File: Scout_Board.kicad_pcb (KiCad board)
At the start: 2 copper layers, 102.5 x 80 mm, 57 parts, among them J1 Conn_01x01_Pin, J2 Conn_01x04_Pin, J3 RAPC722X, J4 Screw_Terminal_01x02, J5 5V, J6 GND, Q1 BSS138, Q2 BSS138, U1 DRV8871DDA, U2 ESP32-S3-DEVKITC-1U-N8R2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

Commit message: New Branch - Alpha2.0
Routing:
- net RxD: track 41.0 -> 40.0 mm

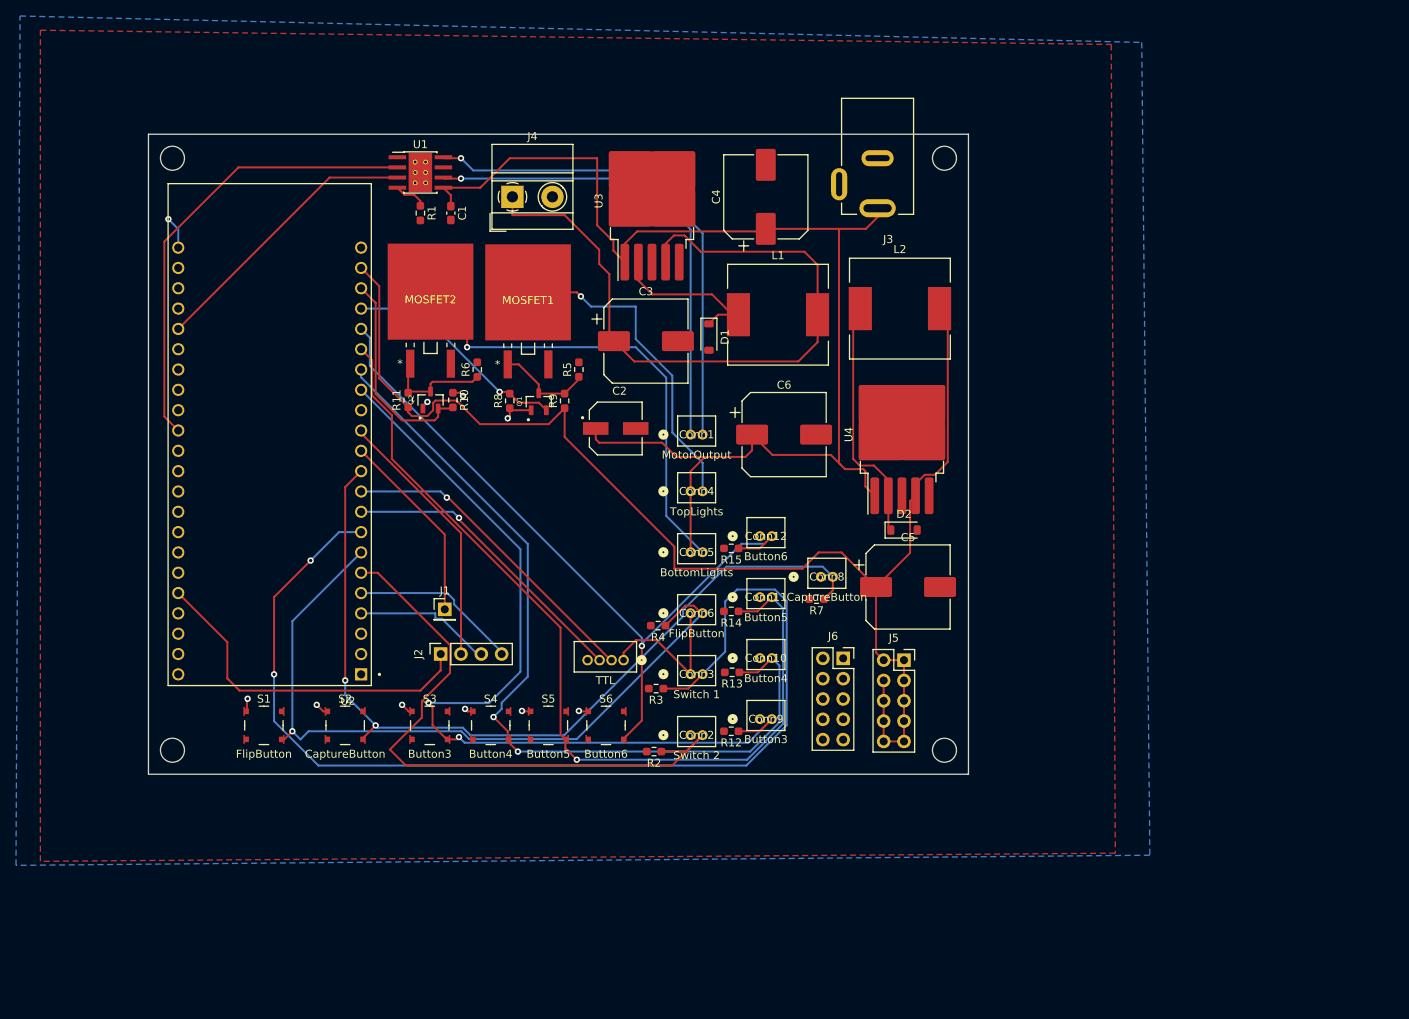
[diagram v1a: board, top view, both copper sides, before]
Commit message: power board changes
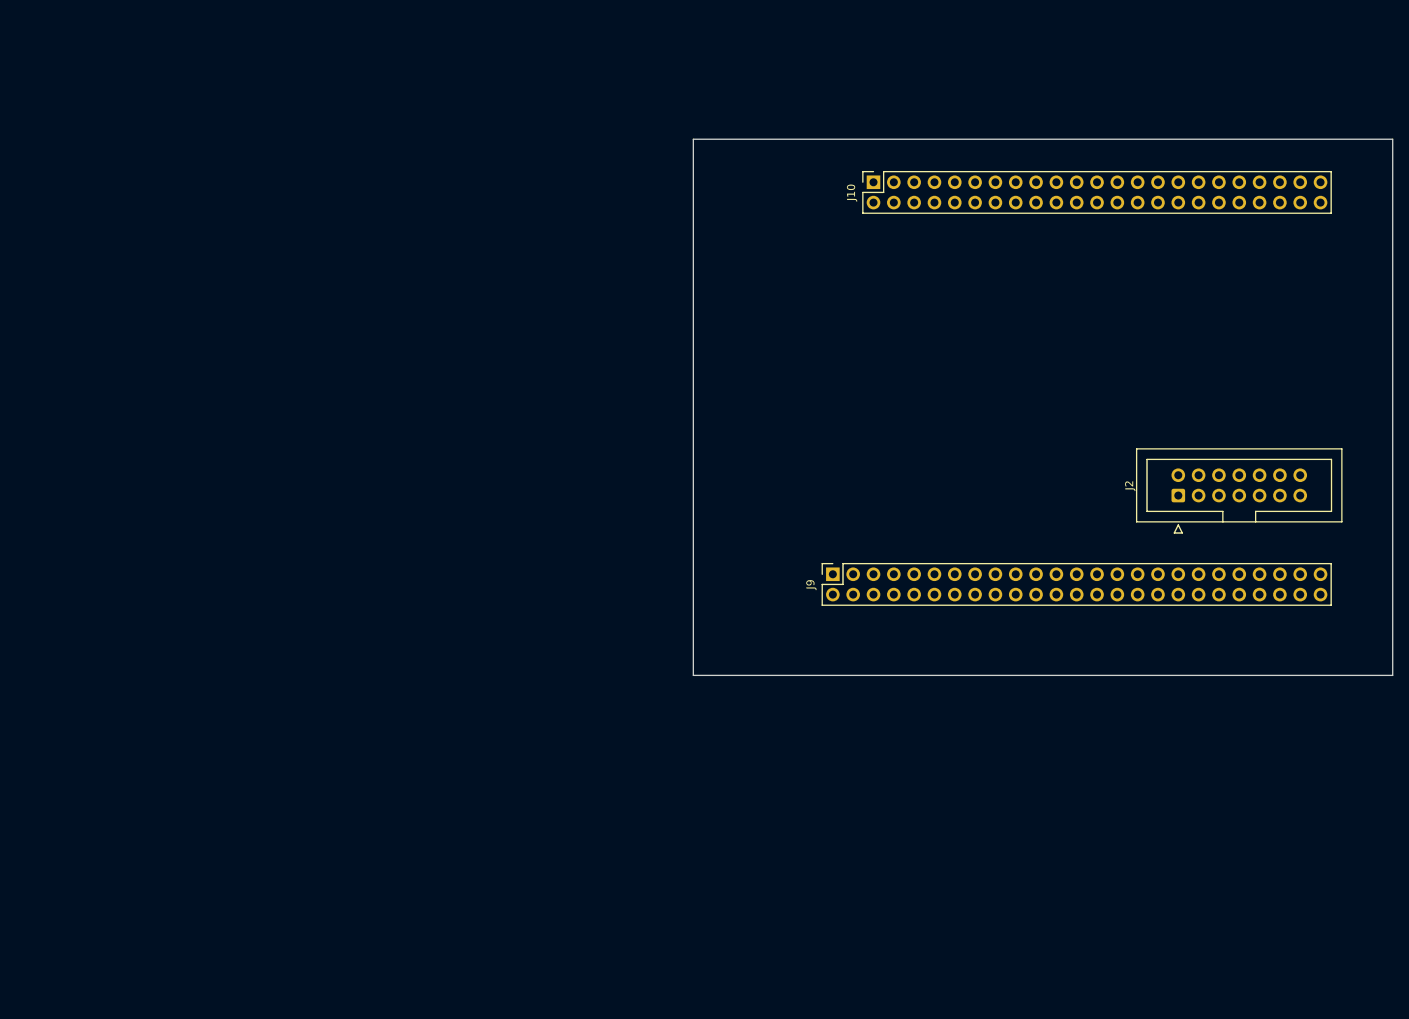
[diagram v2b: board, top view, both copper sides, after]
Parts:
- removed C1: 0.1uF/50V, Capacitor_SMD:C_0603_1608Metric_Pad1.08x0.95mm_HandSolder
- removed C2: 22uF/63V, EEH_ZA1J220XP:CAP_EEHZA1J220XP
- removed C3, C5: 220uF/35V, Capacitor_SMD:CP_Elec_10x10
- removed C4, C6: 100uF/63V, Capacitor_SMD:CP_Elec_10x10
- removed Conn1: MotorOutput, Downloaded_footprints:CONN_B2B-ZRLFSN_JST
- removed Conn10: Button4, Downloaded_footprints:CONN_B2B-ZRLFSN_JST
- removed Conn11: Button5, Downloaded_footprints:CONN_B2B-ZRLFSN_JST
- removed Conn12: Button6, Downloaded_footprints:CONN_B2B-ZRLFSN_JST
- removed Conn2: Switch 2, Downloaded_footprints:CONN_B2B-ZRLFSN_JST
- removed Conn3: Switch 1, Downloaded_footprints:CONN_B2B-ZRLFSN_JST
- removed Conn4: TopLights, Downloaded_footprints:CONN_B2B-ZRLFSN_JST
- removed Conn5: BottomLights, Downloaded_footprints:CONN_B2B-ZRLFSN_JST
- removed Conn6: FlipButton, Downloaded_footprints:CONN_B2B-ZRLFSN_JST
- removed Conn7: TTL, Downloaded_footprints:CONN_B4B-ZRLFSN_JST
- removed Conn8: CaptureButton, Downloaded_footprints:CONN_B2B-ZRLFSN_JST
- removed Conn9: Button3, Downloaded_footprints:CONN_B2B-ZRLFSN_JST
- removed D1, D2: 1N5819HW-7-F, Diode_SMD:D_SOD-123
- removed J1: Conn_01x01_Pin, Connector_PinHeader_2.54mm:PinHeader_1x01_P2.54mm_Vertical
- removed J3: RAPC722X, Downloaded_footprints:SWITCHCRAFT_RAPC722X
- removed J4: Screw_Terminal_01x02, TerminalBlock_MetzConnect:TerminalBlock_MetzConnect_Type011_RT05502HBWC_1x02_P5.00mm_Horizontal
- removed J5: 5V, Connector_PinSocket_2.54mm:PinSocket_2x05_P2.54mm_Vertical
- removed J6: GND, Connector_PinSocket_2.54mm:PinSocket_2x05_P2.54mm_Vertical
- removed L1, L2: 47uH, Inductor_SMD:L_12x12mm_H8mm
- removed MOSFET1, MOSFET2: IRFZ44NSTRLPBF, Downloaded_footprints:D2PAK_INF
- removed Q1, Q2: BSS138, Downloaded_footprints:SOT95P240X111-3N
- removed R1: 30k, Resistor_SMD:R_0603_1608Metric_Pad0.98x0.95mm_HandSolder
- removed R10, R11, R12, R13, R14, R15, R2, R3, R4, R7, R8, R9: 10k, Resistor_SMD:R_0603_1608Metric_Pad0.98x0.95mm_HandSolder
- removed R5, R6: 1M, Resistor_SMD:R_0603_1608Metric_Pad0.98x0.95mm_HandSolder
- removed S1: FlipButton, digikey-footprints:Switch_Tactile_SMD_4.5x4.5mm_TL3315NF160Q
- removed S2: CaptureButton, digikey-footprints:Switch_Tactile_SMD_4.5x4.5mm_TL3315NF160Q
- removed S3: Button3, digikey-footprints:Switch_Tactile_SMD_4.5x4.5mm_TL3315NF160Q
- removed S4: Button4, digikey-footprints:Switch_Tactile_SMD_4.5x4.5mm_TL3315NF160Q
- removed S5: Button5, digikey-footprints:Switch_Tactile_SMD_4.5x4.5mm_TL3315NF160Q
- removed S6: Button6, digikey-footprints:Switch_Tactile_SMD_4.5x4.5mm_TL3315NF160Q
- removed U1: DRV8871DDA, Package_SO:Texas_HTSOP-8-1EP_3.9x4.9mm_P1.27mm_EP2.95x4.9mm_Mask2.4x3.1mm_ThermalVias
- removed U2: ESP32-S3-DEVKITC-1U-N8R2, Downloaded_footprints:XCVR_ESP32-S3-DEVKITC-1U-N8R2
- removed U3, U4: LM2576HVS-5, Package_TO_SOT_SMD:TO-263-5_TabPin3
- added J10: BBAI_P8, Connector_PinSocket_2.54mm:PinSocket_2x23_P2.54mm_Vertical, F.Cu at (226.1, 95.5)
- added J9: BBAI_P9, Connector_PinSocket_2.54mm:PinSocket_2x25_P2.54mm_Vertical, F.Cu at (221.0, 144.5)
- J2: value Conn_01x04_Pin -> Conn_02x07_Odd_Even; footprint Connector_PinSocket_2.54mm:PinSocket_1x04_P2.54mm_Vertical -> Connector_IDC:IDC-Header_2x07_P2.54mm_Vertical
- moved J2 94.3 mm to (264.2, 134.6)
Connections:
- J2 pad 1: Conn1 -> Sw1
- J2 pad 2: Conn2 -> Sw2
- J2 pad 3: Conn3 -> Sw1b
- J2 pad 4: Conn4 -> Sw1b
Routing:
- net +5V: track 169.3 -> 0.00 mm
- net +12V: track 160.4 -> 0.00 mm
- net Sw1: track 138.5 -> 0.00 mm, vias 2 -> 0
- net Button5: track 111.4 -> 0.00 mm, vias 1 -> 0
- net Button3: track 109.2 -> 0.00 mm, vias 2 -> 0
- net CaptureButton: track 107.3 -> 0.00 mm, vias 2 -> 0
- net Button4: track 106.8 -> 0.00 mm, vias 2 -> 0
- net Button6: track 93.7 -> 0.00 mm, vias 1 -> 0
- net FlipButton: track 92.9 -> 0.00 mm, vias 1 -> 0
- net +5VA: track 87.5 -> 0.00 mm
- net Sw2: track 78.5 -> 0.00 mm
- net OUT2: track 61.5 -> 0.00 mm, vias 1 -> 0
- net OUT1: track 59.2 -> 0.00 mm, vias 1 -> 0
- net Net-(Conn5-Pin_2): track 59.0 -> 0.00 mm, vias 1 -> 0
- net IN2: track 57.3 -> 0.00 mm
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- removed copper zone on B.Cu, net +3.3V
- removed copper zone on F.Cu, net GND
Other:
- board size 102.5 x 80 mm -> 87.4 x 67 mm

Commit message: New board test
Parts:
- added C1: 100uF/16V, Capacitor_SMD:CP_Elec_6.3x5.9, F.Cu at (147.0, 169.5)
- added Conn2: CaptureButton, Connector_JST:JST_XH_B2B-XH-AM_1x02_P2.50mm_Vertical, F.Cu at (240.5, 173.0)
- added Conn4: FlipButton, Connector_JST:JST_XH_B2B-XH-AM_1x02_P2.50mm_Vertical, F.Cu at (240.5, 183.0)
- added J1: Conn_01x04_Pin, Connector_PinSocket_2.54mm:PinSocket_1x04_P2.54mm_Vertical, F.Cu at (217.0, 167.4)
- added J11: BBAI_P8, Connector_PinSocket_2.54mm:PinSocket_2x23_P2.54mm_Vertical, F.Cu at (177.8, 182.9)
- added J5: 5V, Connector_PinSocket_2.54mm:PinSocket_2x05_P2.54mm_Vertical, F.Cu at (224.8, 165.9)
- added J6: GND, Connector_PinSocket_2.54mm:PinSocket_2x05_P2.54mm_Vertical, F.Cu at (232.0, 165.9)
- added J7: IN, RAPC722X:SWITCHCRAFT_RAPC722X, F.Cu at (238.2, 145.8)
- added MOSFET1: IRFZ44NSTRLPBF, IRFZ44NSTRLPBF:DPAK254P1524X483-3N, B.Cu at (184.6, 151.0)
- added MOSFET2: IRFZ44NSTRLPBF, IRFZ44NSTRLPBF:DPAK254P1524X483-3N, B.Cu at (197.0, 151.0)
- added Q1: BSS138, BSS138:SOT95P240X111-3N, B.Cu at (164.9, 152.6)
- added Q2: BSS138, BSS138:SOT95P240X111-3N, B.Cu at (164.9, 157.0)
- added R1: 10k, Resistor_SMD:R_0603_1608Metric_Pad0.98x0.95mm_HandSolder, B.Cu at (235.0, 179.0)
- added R10: 1M, Resistor_SMD:R_0603_1608Metric_Pad0.98x0.95mm_HandSolder, B.Cu at (183.9, 161.3)
- added R11: 10k, Resistor_SMD:R_0603_1608Metric_Pad0.98x0.95mm_HandSolder, B.Cu at (169.1, 151.0)
- added R12: 10k, Resistor_SMD:R_0603_1608Metric_Pad0.98x0.95mm_HandSolder, B.Cu at (170.0, 159.0)
- added R13: 1M, Resistor_SMD:R_0603_1608Metric_Pad0.98x0.95mm_HandSolder, B.Cu at (197.0, 162.0)
- added R14: 10k, Resistor_SMD:R_0603_1608Metric_Pad0.98x0.95mm_HandSolder, B.Cu at (170.0, 156.0)
- added R2: 10k, Resistor_SMD:R_0603_1608Metric_Pad0.98x0.95mm_HandSolder, B.Cu at (236.0, 171.0)
- added R7: 10k, Resistor_SMD:R_0603_1608Metric_Pad0.98x0.95mm_HandSolder, B.Cu at (172.0, 175.1)
- added R8: 10k, Resistor_SMD:R_0603_1608Metric_Pad0.98x0.95mm_HandSolder, B.Cu at (172.0, 170.0)
- added R9: 10k, Resistor_SMD:R_0603_1608Metric_Pad0.98x0.95mm_HandSolder, B.Cu at (169.9, 153.0)
- added U1: ESP32-S3-DEVKITC-1U-N8R2, ESP32-S3-DEVKITC-1-N8R2:XCVR_ESP32-S3-DEVKITC-1-N8R2, F.Cu at (187.9, 152.5)
- added U2: ~, Module:Pololu_Breakout-16_15.2x20.3mm, F.Cu at (145.8, 188.0)
- J10: value BBAI_P8 -> BBAI_P9; footprint Connector_PinSocket_2.54mm:PinSocket_2x23_P2.54mm_Vertical -> Connector_PinSocket_2.54mm:PinSocket_2x25_P2.54mm_Vertical
- J9: value BBAI_P9 -> IN; footprint Connector_PinSocket_2.54mm:PinSocket_2x25_P2.54mm_Vertical -> RAPC722X:SWITCHCRAFT_RAPC722X
- moved J2 93.1 mm to (180.3, 175.0)
- moved J10 42.4 mm to (233.7, 137.2), turned to -90 degrees
- moved J9 22.4 mm to (238.2, 158.8)
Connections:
- net BLb renamed +12V
- J2 pad 3: Sw1b -> 5V
- J2 pad 4: Sw1b -> 5V
- J9 pad 1: unconnected-(J9-GND-Pad1) -> 5V
- J9 pad 2: unconnected-(J9-GND-Pad2) -> GND
- J9 pad 3: unconnected-(J9-3.3V-Pad3) -> GND
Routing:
- net TLa: track 0.00 -> 48.0 mm
- net 2B: track 0.00 -> 45.3 mm
- net BottomLightsHV: track 0.00 -> 43.6 mm
- net 2A: track 0.00 -> 40.1 mm
- net BLa: track 0.00 -> 35.2 mm
- net 1A: track 0.00 -> 34.4 mm
- net TopLightsHV: track 0.00 -> 33.2 mm
- net GND: track 0.00 -> 30.7 mm
- net +3.3V: track 0.00 -> 29.5 mm, vias 0 -> 1
- net 1B: track 0.00 -> 29.0 mm
- net Sw2: track 0.00 -> 8.94 mm
- net FlipButton: track 0.00 -> 8.74 mm
- net Sw1: track 0.00 -> 8.64 mm
- net CaptureButton: track 0.00 -> 8.21 mm
- net +12V: track 0.00 -> 6.98 mm
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- added copper zone on F.Cu, net +12V
- added copper zone on B.Cu, net +3.3V
- added copper zone on In1.Cu, net +3.3V
- added copper zone on In2.Cu, net 5V
- added copper zone on B.Cu, net GND
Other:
- board size 87.4 x 67 mm -> 104.2 x 65 mm
- copper layers 2 -> 4

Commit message: Layout changes
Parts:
- removed J5: 5V, Connector_PinSocket_2.54mm:PinSocket_2x05_P2.54mm_Vertical
- removed J6: GND, Connector_PinSocket_2.54mm:PinSocket_2x05_P2.54mm_Vertical
- removed J7, J9: IN, RAPC722X:SWITCHCRAFT_RAPC722X
- added J3: 705530002, 705530002:CONN3_53-0002_MOL, F.Cu at (254.0, 132.1)
- added MOSFET3: IRFZ44NSTRLPBF, IRFZ44NSTRLPBF:DPAK254P1524X483-3N, B.Cu at (180.3, 165.1)
- added Q3: BSS138, BSS138:SOT95P240X111-3N, B.Cu at (222.2, 160.5)
- added R29: 10k, Resistor_SMD:R_0603_1608Metric_Pad0.98x0.95mm_HandSolder, B.Cu at (225.6, 160.5)
- added R30: 1M, Resistor_SMD:R_0603_1608Metric_Pad0.98x0.95mm_HandSolder, B.Cu at (218.2, 158.6)
- added R31: 10k, Resistor_SMD:R_0603_1608Metric_Pad0.98x0.95mm_HandSolder, B.Cu at (218.2, 161.8)
- moved U2 101.9 mm to (247.7, 184.1)
- moved C1 99.2 mm to (246.1, 165.1)
- moved R7 90.1 mm to (256.9, 144.8), turned to 0 degrees
- moved R8 87.9 mm to (256.9, 147.3), turned to 0 degrees
- moved J2 75.0 mm to (248.9, 144.8), turned to -90 degrees
- moved Conn2 68.7 mm to (177.8, 144.8)
- moved Q1 60.3 mm to (221.7, 172.9)
- moved R9 59.1 mm to (225.6, 172.9), turned to -90 degrees
- moved Conn4 58.9 mm to (195.6, 144.8)
- moved Q2 57.6 mm to (221.7, 166.4)
- moved J1 57.1 mm to (170.2, 134.6)
- moved R2 56.2 mm to (185.7, 145.9)
- moved R12 56.0 mm to (225.5, 166.5), turned to -90 degrees
- moved J10 55.9 mm to (177.8, 134.5), turned to 90 degrees
- moved R11 54.0 mm to (218.0, 173.9), turned to 0 degrees
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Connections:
- J2 pad 11: +12V -> BL-
- J2 pad 13: unconnected-(J2-Pin_13-Pad13) -> UV-
- J2 pad 5: TLa -> +12V
- J2 pad 9: BLa -> TL-
- MOSFET1 pad 2: TLa -> TL-
- MOSFET2 pad 2: BLa -> BL-
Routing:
- net TL-: track 0.00 -> 114.6 mm
- net BL-: track 0.00 -> 96.0 mm
- net UV-: track 0.00 -> 64.1 mm
- net TLa: track 48.0 -> 0.00 mm
- net UVLightsHV: track 0.00 -> 45.6 mm
- net BLa: track 35.2 -> 0.00 mm
- net GND: track 30.7 -> 59.2 mm, vias 0 -> 4
- net TopLightsHV: track 33.2 -> 16.5 mm
- net 2B: track 45.3 -> 31.0 mm
- net BottomLightsHV: track 43.6 -> 31.1 mm
- net 2A: track 40.1 -> 31.0 mm
- net 1A: track 34.4 -> 31.0 mm
- net FlipButton: track 8.74 -> 5.35 mm
- net 5V: track 3.09 -> 0.00 mm, vias 2 -> 0
- net CaptureButton: track 8.21 -> 5.44 mm
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- added copper zone on In1.Cu, net +12V
- added copper zone on In2.Cu, net +3.3V
- added copper zone on B.Cu, net 5V
- added copper zone on F.Cu, net GND
- removed copper zone on F.Cu, net +12V
- removed copper zone on B.Cu, net +3.3V
- removed copper zone on In1.Cu, net +3.3V
- removed copper zone on In2.Cu, net 5V
- removed copper zone on B.Cu, net GND
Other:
- board size 104.2 x 65 mm -> 104.1 x 61 mm

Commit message: Layout updated with mounting holes
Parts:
- added J7: I2C, digikey-footprints:PinHeader_1x2_P2.5mm_Drill1.1mm, F.Cu at (170.4, 130.6)
- added J8: SPI, digikey-footprints:PinHeader_1x4_P2.5mm_Drill1.1mm, F.Cu at (245.6, 137.8)
- moved R7 28.9 mm to (228.6, 150.7), turned to -90 degrees
- moved R8 24.7 mm to (232.4, 150.7), turned to -90 degrees
- moved R11 13.1 mm to (230.2, 169.3), turned to 90 degrees
- moved R9 11.8 mm to (229.3, 161.8), turned to 0 degrees
- moved R30 10.9 mm to (215.0, 169.1), turned to -90 degrees
- moved Q1 10.5 mm to (229.3, 165.6), turned to -90 degrees
- moved R10 9.95 mm to (227.7, 169.4), turned to -90 degrees
- moved R29 8.72 mm to (216.9, 161.8), turned to 0 degrees
- moved R31 7.32 mm to (218.2, 169.1), turned to 90 degrees
- moved Q3 7.04 mm to (216.9, 165.1), turned to -90 degrees
- moved R13 6.26 mm to (224.0, 169.3), turned to -90 degrees
- moved R14 5.46 mm to (221.2, 169.3), turned to 90 degrees
- moved R12 5.39 mm to (222.9, 161.8), turned to 0 degrees
- moved J1 4.06 mm to (170.2, 138.7)
- moved Q2 1.39 mm to (222.8, 165.6), turned to -90 degrees
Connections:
- J10 pad 10: unconnected-(J10-Reset-Pad10) -> Sys_reset
- J10 pad 16: unconnected-(J10-GPIO0_94-Pad16) -> I2C1_SDA
- J10 pad 17: unconnected-(J10-GPIO0_28-Pad17) -> I2C1_SCL
- J10 pad 24: unconnected-(J10-GPIO0_119-Pad24) -> TxD
- J10 pad 26: unconnected-(J10-GPIO0_118-Pad26) -> RxD
- J10 pad 28: unconnected-(J10-GPIO1_11-Pad28) -> SPI1_CS0
- J10 pad 29: unconnected-(J10-GPIO1_14-Pad29) -> SPI1_D0
- J10 pad 30: unconnected-(J10-GPIO1_13-Pad30) -> SPI1_D1
- J10 pad 31: unconnected-(J10-GPIO1_12-Pad31) -> SPI1_SCLK
- J10 pad 43: unconnected-(J10-GND-Pad43) -> GND
- J10 pad 44: unconnected-(J10-GND-Pad44) -> GND
- J10 pad 45: unconnected-(J10-GND-Pad45) -> GND
- J10 pad 46: unconnected-(J10-GND-Pad46) -> GND
- J11 pad 1: unconnected-(J11-GND-Pad1) -> GND
- J11 pad 2: unconnected-(J11-GND-Pad2) -> GND
- J11 pad 7: unconnected-(J11-GPIO0_15-Pad7) -> SBC_Power
- J11 pad 8: unconnected-(J11-GPIO0_14-Pad8) -> Wire1
- J11 pad 9: unconnected-(J11-GPIO0_17-Pad9) -> Wire2
- J2 pad 1: Sw1 -> TL-
- J2 pad 11: BL- -> UV-
- J2 pad 13: UV- -> Sw1
- J2 pad 14: unconnected-(J2-Pin_14-Pad14) -> Sw2
- J2 pad 2: Sw2 -> unconnected-(J2-Pin_2-Pad2)
- J2 pad 9: TL- -> BL-
- U1 pad J1_12: unconnected-(U1-GPIO8-PadJ1_12) -> RxD
- U1 pad J1_13: unconnected-(U1-GPIO3-PadJ1_13) -> TxD
- U1 pad J1_14: unconnected-(U1-GPIO46-PadJ1_14) -> Sys_reset
- U1 pad J1_15: unconnected-(U1-GPIO9-PadJ1_15) -> Conn1
- U1 pad J1_16: unconnected-(U1-GPIO10-PadJ1_16) -> Conn2
- U1 pad J1_17: unconnected-(U1-GPIO11-PadJ1_17) -> Conn3
- U1 pad J1_18: unconnected-(U1-GPIO12-PadJ1_18) -> Conn4
- U1 pad J1_19: unconnected-(U1-GPIO13-PadJ1_19) -> FlipButton
- U1 pad J1_20: unconnected-(U1-GPIO14-PadJ1_20) -> CaptureButton
- U1 pad J1_4: unconnected-(U1-GPIO4-PadJ1_4) -> Sw2
- U1 pad J1_5: unconnected-(U1-GPIO5-PadJ1_5) -> Sw1
- U1 pad J1_6: unconnected-(U1-GPIO6-PadJ1_6) -> TopLightsLV
- U1 pad J1_7: unconnected-(U1-GPIO7-PadJ1_7) -> BottomLightsLV
- U1 pad J1_8: unconnected-(U1-GPIO15-PadJ1_8) -> UVLightsLV
- U1 pad J3_10: unconnected-(U1-GPIO38-PadJ3_10) -> RST/SDO
- U1 pad J3_18: unconnected-(U1-GPIO21-PadJ3_18) -> Wire2
- U1 pad J3_19: unconnected-(U1-USB_D+/GPIO20-PadJ3_19) -> SBC_Power
- U1 pad J3_2: unconnected-(U1-U0TXD/GPIO43-PadJ3_2) -> EN
- U1 pad J3_20: unconnected-(U1-USB_D-/GPIO19-PadJ3_20) -> Wire1
- U1 pad J3_3: unconnected-(U1-U0RXD/GPIO44-PadJ3_3) -> MS1/SDI
- U1 pad J3_5: unconnected-(U1-GPIO2-PadJ3_5) -> MS2/SCK
- U1 pad J3_6: unconnected-(U1-MTMS/GPIO42-PadJ3_6) -> MS3/CS
- U1 pad J3_7: unconnected-(U1-MTDI/GPIO41-PadJ3_7) -> SLP/NC
- U1 pad J3_8: unconnected-(U1-MTDO/GPIO40-PadJ3_8) -> STEP
- U1 pad J3_9: unconnected-(U1-MTCK/GPIO39-PadJ3_9) -> DIR
- U2 pad 6: unconnected-(U2-SLP/NC-Pad6) -> SLP/NC
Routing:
- net DIR: track 0.00 -> 59.2 mm
- net RST/SDO: track 0.00 -> 54.6 mm
- net STEP: track 0.00 -> 53.8 mm
- net SLP/NC: track 0.00 -> 48.3 mm
- net Conn1: track 0.00 -> 45.9 mm
- net MS3/CS: track 0.00 -> 41.1 mm
- net 5V: track 0.00 -> 40.8 mm, vias 0 -> 4
- net Conn2: track 0.00 -> 39.6 mm
- net SPI1_CS0: track 0.00 -> 36.3 mm
- net MS2/SCK: track 0.00 -> 35.7 mm
- net SPI1_D0: track 0.00 -> 34.4 mm
- net SPI1_D1: track 0.00 -> 34.0 mm
- net Conn3: track 0.00 -> 33.3 mm
- net SPI1_SCLK: track 0.00 -> 30.8 mm
- net I2C1_SCL: track 0.00 -> 29.3 mm
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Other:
- outline, holes or cut-outs redrawn
- board text added: "12V"
- board text added: "23"
- board text added: "5V"
- board text added: "Gnd"
